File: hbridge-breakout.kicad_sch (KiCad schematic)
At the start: 15 parts, among them J1 Conn_01x10, J2 Conn_01x04, J3 Conn_01x08, U1 74HC00, U2 DRV8870DDA

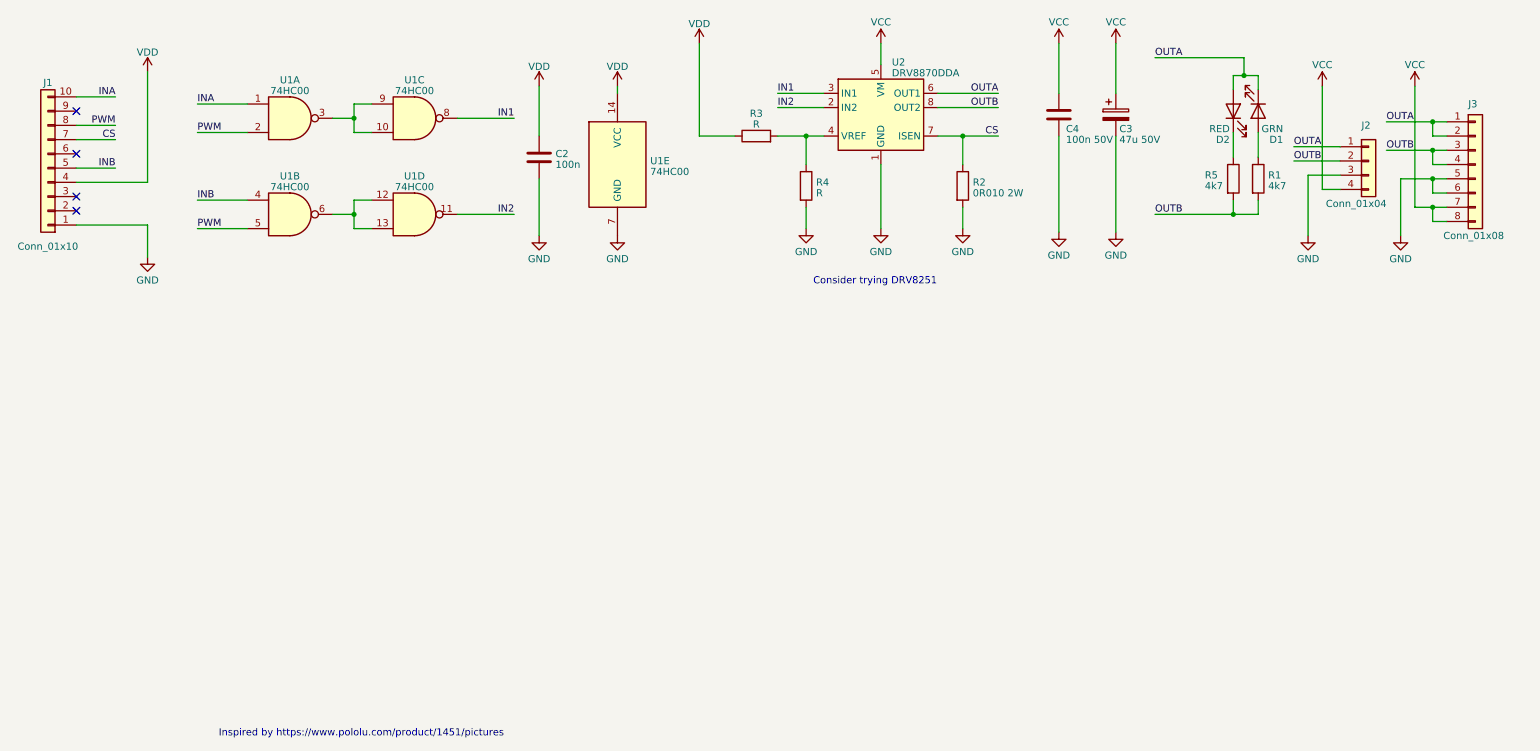
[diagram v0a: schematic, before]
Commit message: Fixed a terrible bug where the power input/outputs at the bottom of the board were flipped.
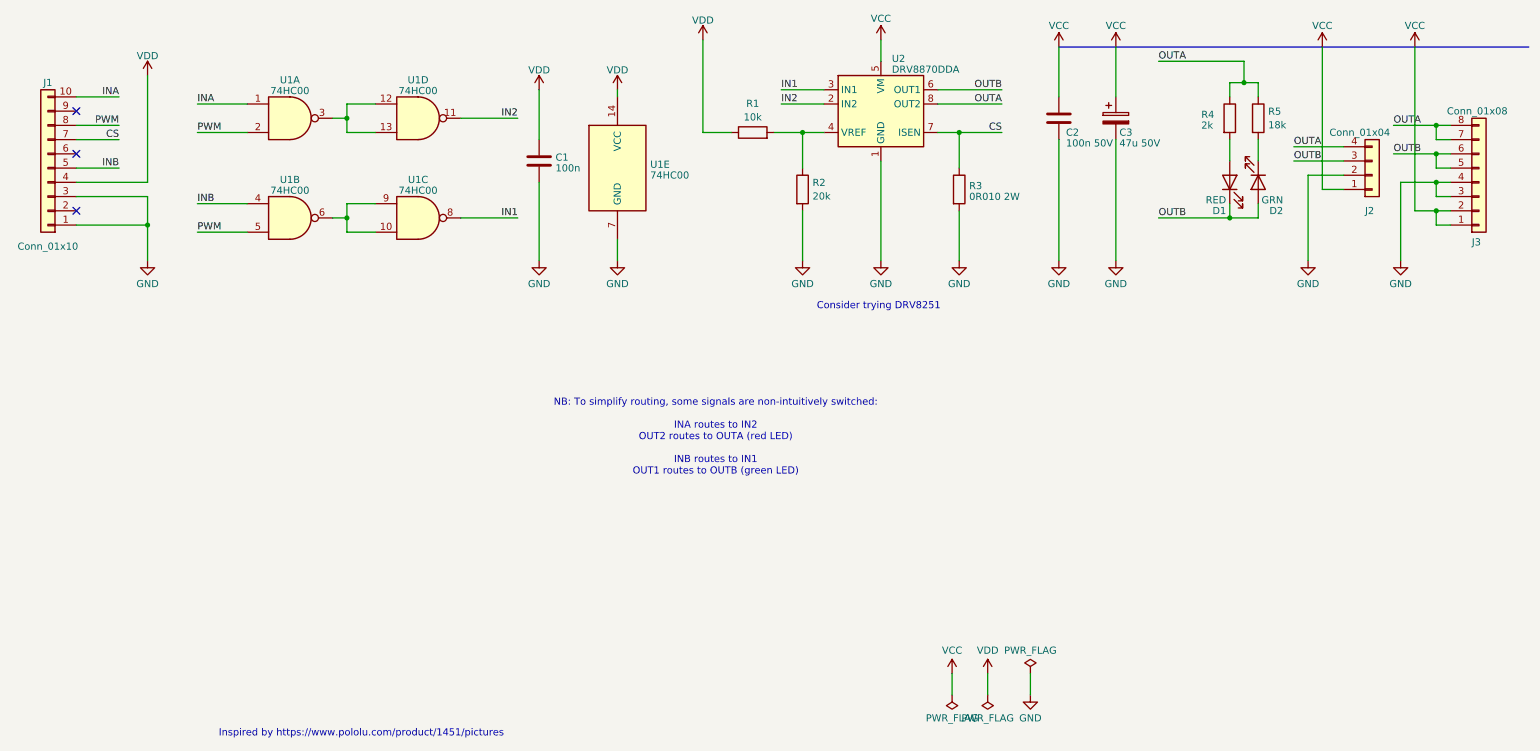
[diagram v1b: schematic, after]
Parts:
- R1: renamed from R3; value R -> 10k
- R2: renamed from R4; value R -> 20k
- R4: renamed from R5; value 4k7 -> 2k
- R5: renamed from R1; value 4k7 -> 18k
- renumbered C2 to C1, C4 to C2, D2 to D1, D1 to D2, R2 to R3
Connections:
- net GND: now also J1.3 (Pin_3), J2.2 (Pin_2), J3.3 (Pin_3), J3.4 (Pin_4); no longer J2.3 (Pin_3), J3.5 (Pin_5), J3.6 (Pin_6)
- net OUTA: now also J2.4 (Pin_4), J3.7 (Pin_7), J3.8 (Pin_8), R4.1, R5.1, U2.8 (OUT2); no longer D1.2 (A), D2.1 (K), J2.1 (Pin_1), J3.1 (Pin_1), J3.2 (Pin_2), U2.6 (OUT1)
- net OUTB: now also D1.1 (K), D2.2 (A), J2.3 (Pin_3), J3.5 (Pin_5), J3.6 (Pin_6), U2.6 (OUT1); no longer J2.2 (Pin_2), J3.3 (Pin_3), J3.4 (Pin_4), R4.2, R5.2, U2.8 (OUT2)
- net VCC: now also J2.1 (Pin_1), J3.1 (Pin_1), J3.2 (Pin_2); no longer J2.4 (Pin_4), J3.7 (Pin_7), J3.8 (Pin_8)
- net at U1.12, U1.13: now also U1.3; no longer U1.6
- net at U1.10, U1.9: now also U1.6; no longer U1.3
- new net: D2.1 (K), R5.2
- new net: D1.2 (A), R4.2
- no-connect marks 4 -> 3
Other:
- note added: "NB: To simplify routing, some signals are non-intuitively switched: INA routes to IN2 OUT2 routes to OUTA (red LED) INB routes to IN1 OUT1 routes to OUTB (green LED)"
- moved on the sheet: C1, C2, C3, D1, D2, J2, J3, R1, R2, R3, R4, R5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
